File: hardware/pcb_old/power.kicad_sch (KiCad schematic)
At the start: 53 parts, among them J1 XT30PW-F, J12 Solar, J13 USB-C, U1 AP63205, U11 USBLC6, U12 TP5100, U7 CN3722, U8 MT3608

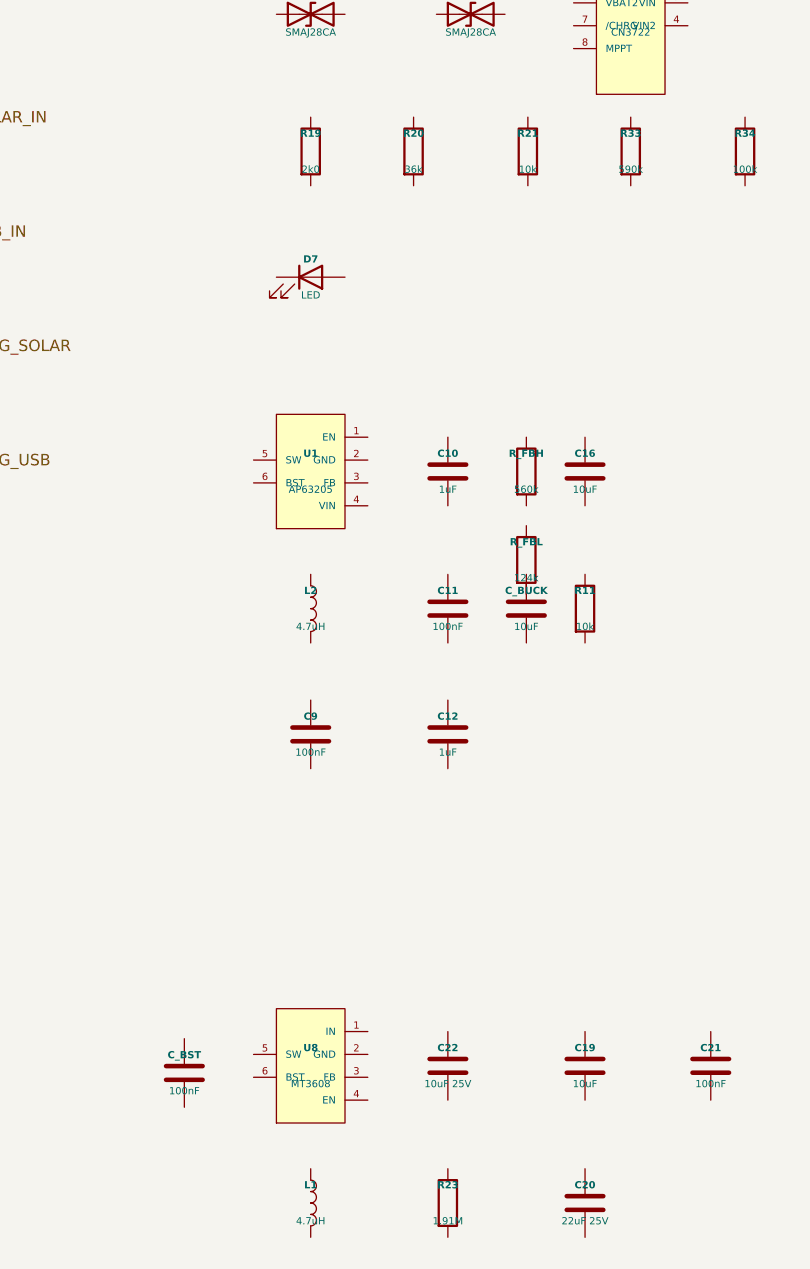
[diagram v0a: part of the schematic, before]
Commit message: hw(pcb): fresh-start PCB — fix 4 critical schematic gaps, add wiring/placement docs
Archive old auto-generated PCB to hardware/pcb_old/. Start clean hardware/pcb/
with reference-only design documents for manual KiCad layout.

Critical electrical fixes:
- Add R_FBH (560kΩ) and R_FBL (124kΩ) symbols to power.kicad_sch — AP63205WU
  was missing its FB divider entirely; without it VOUT floats to rail and destroys
  the ESP32 on first power-on. Sets VOUT = 3.31V.
- Add R_DRDY (4.7kΩ) symbol to sensors.kicad_sch — ADS1115 ALERT/DRDY is
  open-drain and required an external pull-up; firmware was missing edges
  intermittently (root cause of bug fixed in adf7101).
- Add C_BST (100nF) symbol to power.kicad_sch — MT3608B BST→SW bootstrap
  cap is mandatory for gate driver; was ambiguous/missing.
- Add C_BUCK (10µF 0805) symbol to power.kicad_sch — AP63205WU primary output
  filter cap was absent from schematic.
- R33 already corrected from 604kΩ → 590kΩ (CN3722 CV 8.48V → 8.31V, safe for 2S).

New reference documents:
- bom_footprints.md — full BOM with KiCad 10 footprints, LCSC codes, PCBWay notes
- placement_constraints.md — must-be-near/apart rules from datasheets
- schematic_connections.md — net-by-net pin connectivity (authoritative wiring ref
  because schematic has symbols but zero wire connections yet)
- kicad_guide_eli5.md — step-by-step KiCad 10 setup guide including scripting console
- kicad_place_script.py — PCB editor scripting console auto-placement script
- senior_review_2026-05-25.md — senior reviewer report (BLOCKED, 4 CRITICAL)

CLAUDE.md: add electrical correctness gate to /improve cycle to catch missing
companion passives before tape-out.

Co-Authored-By: Claude Sonnet 4.6 <noreply@anthropic.com>
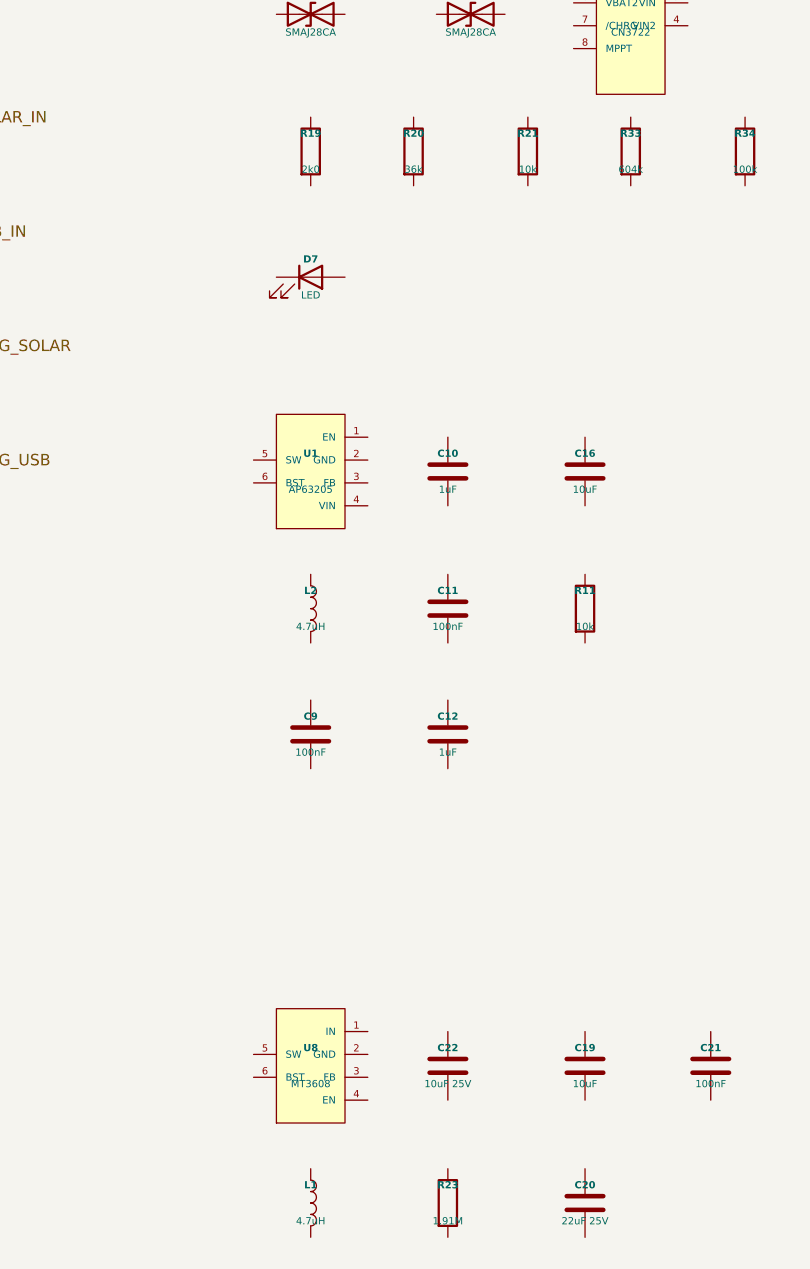
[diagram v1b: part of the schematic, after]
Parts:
- removed C_BST: 100nF, Capacitor_SMD:C_0402_1005Metric, symbol Device:C
- removed C_BUCK: 10uF, Capacitor_SMD:C_0805_2012Metric, symbol Device:C
- removed R_FBH: 560k, Resistor_SMD:R_0402_1005Metric, symbol Device:R
- removed R_FBL: 124k, Resistor_SMD:R_0402_1005Metric, symbol Device:R
- R33: value 590k -> 604k
